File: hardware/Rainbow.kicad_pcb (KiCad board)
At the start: 2 copper layers, 63.3 x 47.9 mm, 22 parts, among them J1 PICKit3, J2 UART, J3 BARREL_JACK, J4 HC-05, J5 RGB, Q1 Q_NMOS_GDS, Q2 Q_NMOS_GDS, Q3 Q_NMOS_GDS, SW1 SWITCH, U1 PIC16F15325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

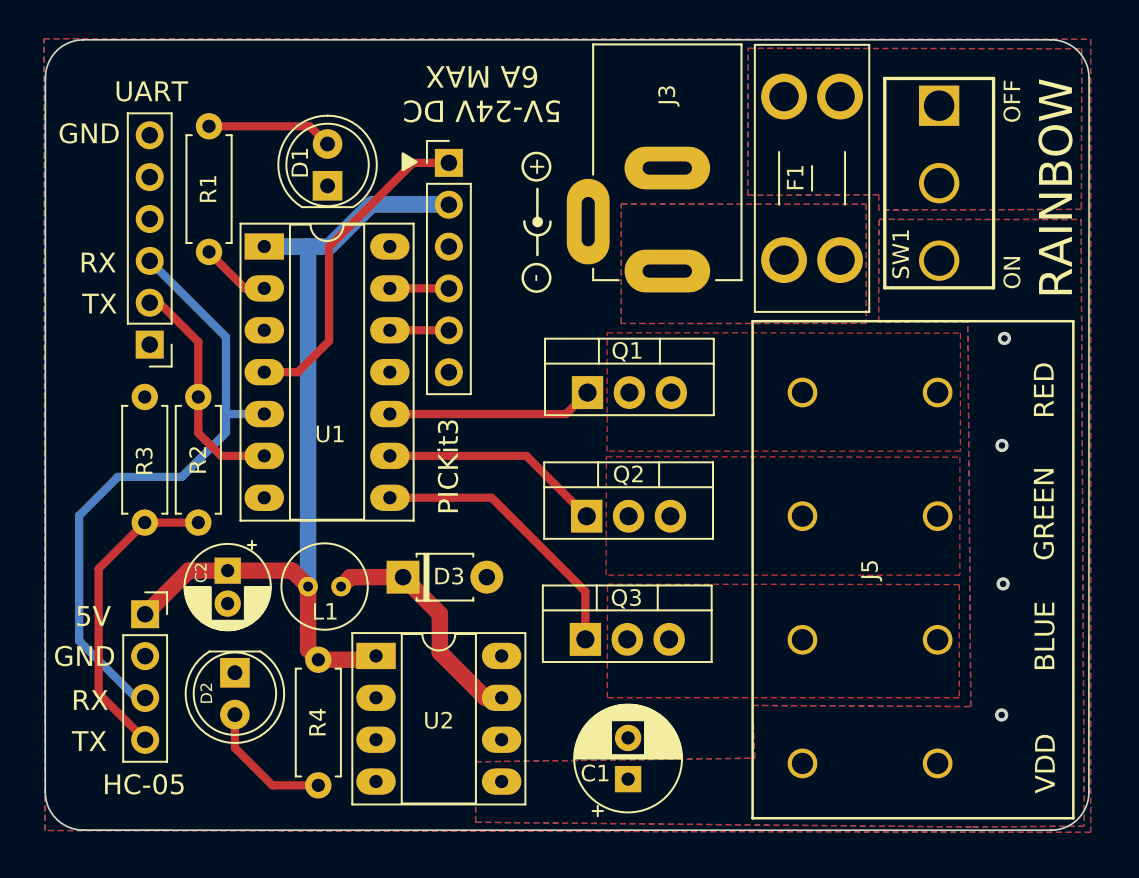
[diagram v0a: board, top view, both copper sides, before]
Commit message: 0.1 uF bypass capacitor
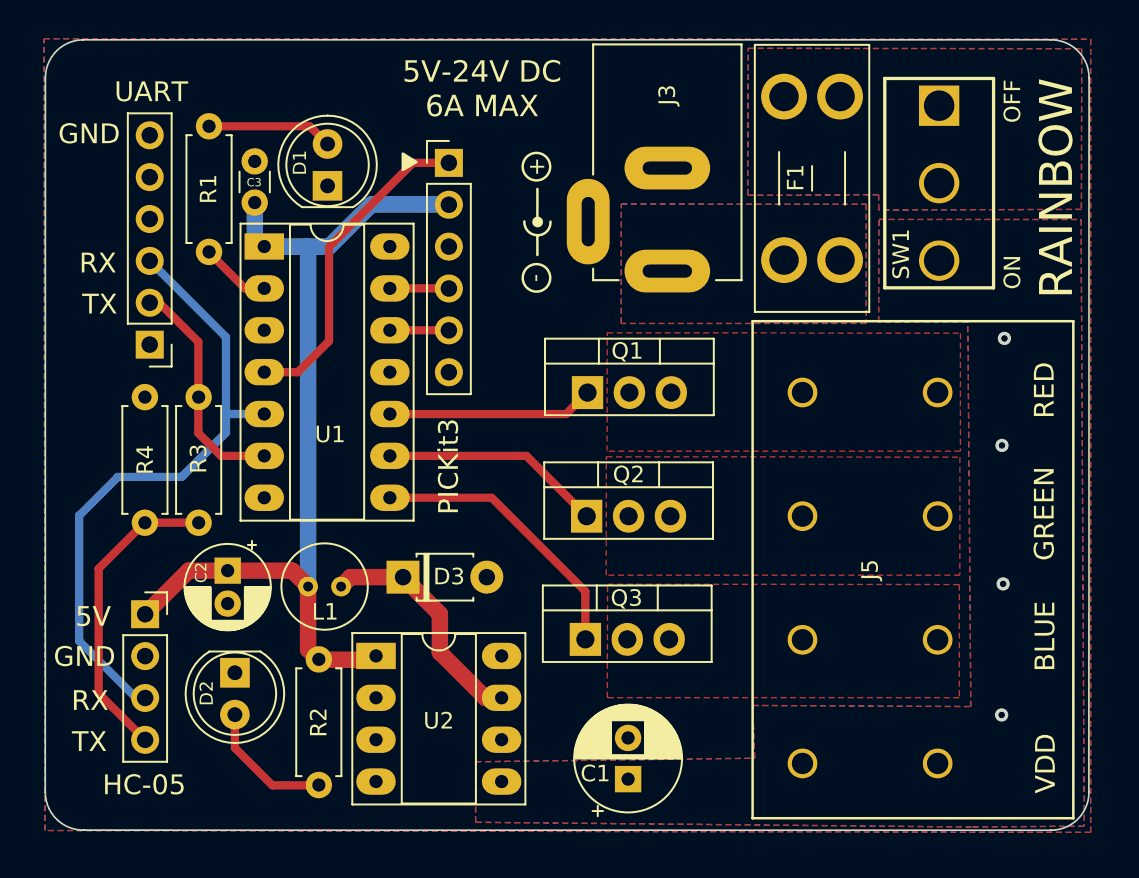
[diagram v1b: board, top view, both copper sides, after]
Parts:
- added C3: 0.1uF, Capacitor_THT:C_Disc_D3.0mm_W1.6mm_P2.50mm, F.Cu at (124.6, 73.2)
- R2: value 1K -> 270R
- R3: value 2K -> 1K
- R4: value 270R -> 2K
- moved R2 17.5 mm to (128.5, 100.9)
- moved R4 13.4 mm to (118.0, 92.7), turned to 90 degrees
- moved R3 8.28 mm to (121.2, 85.0), turned to -90 degrees
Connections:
- R2 pad 1: TX -> +5V
- R2 pad 2: Net-(J4-Pad4) -> Net-(D2-Pad2)
- R3 pad 1: Net-(J4-Pad4) -> TX
- R3 pad 2: GNDREF -> Net-(J4-Pad4)
- R4 pad 1: +5V -> Net-(J4-Pad4)
- R4 pad 2: Net-(D2-Pad2) -> GNDREF
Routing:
- net +5V: track 52.2 -> 55.1 mm
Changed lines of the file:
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@@
+    )
+  )
+  (footprint "Capacitor_THT:C_Disc_D3.0mm_W1.6mm_P2.50mm" (layer "F.Cu")
+    (at 124.63 73.23 90)
+    (descr "C, Disc series, Radial, pin pitch=2.50mm, , diameter*width=3.0*1.6mm^2, Capacitor, http://www.vishay.com/docs/45233/krseries.pdf")
+    (tags "C Disc series Radial pin pitch 2.50mm  diameter 3.0mm width 1.6mm Capacitor")
+    (property "Sheetfile" "Rainbow.kicad_sch")
+    (property "Sheetname" "")
+    (attr through_hole)
+    (fp_text reference "C3" (at 1.22 -0.03 180) (layer "F.SilkS")
+      (effects (font (size 0.5 0.5) (thickness 0.1)))
+    )
+    (fp_text value "0.1uF" (at 1.25 2.05 90) (layer "F.Fab")
+      (effects (font (size 1 1) (thickness 0.15)))
+    )
+    (fp_text user "${REFERENCE}" (at 1.25 0 90) (layer "F.Fab")
+      (effects (font (size 0.6 0.6) (thickness 0.09)))
+    )
+    (fp_line (start 0.621 -0.92) (end 1.879 -0.92) (layer "F.SilkS") (width 0.12))
+    (fp_line (start 0.621 0.92) (end 1.879 0.92) (layer "F.SilkS") (width 0.12))
+    (fp_line (start 3.55 -1.05) (end -1.05 -1.05) (layer "F.CrtYd") (width 0.05))
+    (fp_line (start 3.55 1.05) (end 3.55 -1.05) (layer "F.CrtYd") (width 0.05))
+    (fp_line (start -1.05 1.05) (end 3.55 1.05) (layer "F.CrtYd") (width 0.05))
+    (fp_line (start -1.05 -1.05) (end -1.05 1.05) (layer "F.CrtYd") (width 0.05))
+    (fp_line (start -0.25 -0.8) (end -0.25 0.8) (layer "F.Fab") (width 0.1))
+    (fp_line (start 2.75 0.8) (end 2.75 -0.8) (layer "F.Fab") (width 0.1))
+    (fp_line (start -0.25 0.8) (end 2.75 0.8) (layer "F.Fab") (width 0.1))
+    (fp_line (start 2.75 -0.8) (end -0.25 -0.8) (layer "F.Fab") (width 0.1))
+    (pad "1" thru_hole circle (at 0 0 90) (size 1.6 1.6) (drill 0.8) (layers *.Cu *.Mask)
+      (net 4 "+5V") (pintype "passive"))
+    (pad "2" thru_hole circle (at 2.5 0 90) (size 1.6 1.6) (drill 0.8) (layers *.Cu *.Mask)
+      (net 1 "GNDREF") (pintype "passive"))
+    (model "${KICAD6_3DMODEL_DIR}/Capacitor_THT.3dshapes/C_Disc_D3.0mm_W1.6mm_P2.50mm.wrl"
+      (offset (xyz 0 0 0))
+      (scale (xyz 1 1 1))
+      (rotate (xyz 0 0 0))
     )
   )
   (footprint "Resistor_THT:R_Axial_DIN0207_L6.3mm_D2.5mm_P7.62mm_Horizontal" (layer "F.Cu")
-    (at 128.49 100.96 -90)
+    (at 117.97 92.65 90)
     (descr "Resistor, Axial_DIN0207 series, Axial, Horizontal, pin pitch=7.62mm, 0.25W = 1/4W, length*diameter=6.3*2.5mm^2, http://cdn-reichelt.de/documents/datenblatt/B400/1_4W%23YAG.pdf")
     (tags "Resistor Axial_DIN0207 series Axial Horizontal pin pitch 7.62mm 0.25W = 1/4W length 6.3mm diameter 2.5mm")
@@
       (effects (font (size 1 1) (thickness 0.15)))
     )
-    (fp_text value "270R" (at 3.81 2.37 90) (layer "F.Fab")
+    (fp_text value "2K" (at 3.81 2.37 90) (layer "F.Fab")
       (effects (font (size 1 1) (thickness 0.15)))
     )
@@
     (fp_line (start 0.66 -1.25) (end 0.66 1.25) (layer "F.Fab") (width 0.1))
     (fp_line (start 0.66 1.25) (end 6.96 1.25) (layer "F.Fab") (width 0.1))
-    (pad "1" thru_hole circle (at 0 0 270) (size 1.6 1.6) (drill 0.8) (layers *.Cu *.Mask)
-      (net 4 "+5V") (pintype "passive"))
-    (pad "2" thru_hole oval (at 7.62 0 270) (size 1.6 1.6) (drill 0.8) (layers *.Cu *.Mask)
-      (net 21 "Net-(D2-Pad2)") (pintype "passive"))
+    (pad "1" thru_hole circle (at 0 0 90) (size 1.6 1.6) (drill 0.8) (layers *.Cu *.Mask)
+      (net 24 "Net-(J4-Pad4)") (pintype "passive"))
+    (pad "2" thru_hole oval (at 7.62 0 90) (size 1.6 1.6) (drill 0.8) (layers *.Cu *.Mask)
+      (net 1 "GNDREF") (pintype "passive"))
     (model "${KICAD6_3DMODEL_DIR}/Resistor_THT.3dshapes/R_Axial_DIN0207_L6.3mm_D2.5mm_P7.62mm_Horizontal.wrl"
       (offset (xyz 0 0 0))
@@
     (attr through_hole)
     (fp_text reference "D2" (at 1.245 1.71 90) (layer "F.SilkS")
-      (effects (font (size 0.7 0.7) (thickness 0.15)))
+      (effects (font (size 0.8 0.8) (thickness 0.125)))
     )
     (fp_text value "LED" (at 1.27 3.96 90) (layer "F.Fab")
@@
     (property "Sheetname" "")
     (attr through_hole)
-    (fp_text reference "D1" (at 1.4 -1.65 90) (layer "F.SilkS")
-      (effects (font (size 1 1) (thickness 0.15)))
+    (fp_text reference "D1" (at 1.405 -1.68 90) (layer "F.SilkS")
+      (effects (font (size 0.8 0.8) (thickness 0.125)))
     )
     (fp_text value "LED" (at 1.27 3.96 90) (layer "F.Fab")
@@
   )
   (footprint "Resistor_THT:R_Axial_DIN0207_L6.3mm_D2.5mm_P7.62mm_Horizontal" (layer "F.Cu")
-    (at 121.21 85.02 -90)
+    (at 128.52 100.94 -90)
     (descr "Resistor, Axial_DIN0207 series, Axial, Horizontal, pin pitch=7.62mm, 0.25W = 1/4W, length*diameter=6.3*2.5mm^2, http://cdn-reichelt.de/documents/datenblatt/B400/1_4W%23YAG.pdf")
     (tags "Resistor Axial_DIN0207 series Axial Horizontal pin pitch 7.62mm 0.25W = 1/4W length 6.3mm diameter 2.5mm")
@@
       (effects (font (size 1 1) (thickness 0.15)))
     )
-    (fp_text value "1K" (at 3.81 2.37 90) (layer "F.Fab")
+    (fp_text value "270R" (at 3.81 2.37 90) (layer "F.Fab")
       (effects (font (size 1 1) (thickness 0.15)))
     )
@@
     (fp_line (start 6.96 1.25) (end 6.96 -1.25) (layer "F.Fab") (width 0.1))
     (pad "1" thru_hole circle (at 0 0 270) (size 1.6 1.6) (drill 0.8) (layers *.Cu *.Mask)
-      (net 9 "TX") (pintype "passive"))
+      (net 4 "+5V") (pintype "passive"))
     (pad "2" thru_hole oval (at 7.62 0 270) (size 1.6 1.6) (drill 0.8) (layers *.Cu *.Mask)
-      (net 24 "Net-(J4-Pad4)") (pintype "passive"))
+      (net 21 "Net-(D2-Pad2)") (pintype "passive"))
     (model "${KICAD6_3DMODEL_DIR}/Resistor_THT.3dshapes/R_Axial_DIN0207_L6.3mm_D2.5mm_P7.62mm_Horizontal.wrl"
       (offset (xyz 0 0 0))
@@
   )
   (footprint "Resistor_THT:R_Axial_DIN0207_L6.3mm_D2.5mm_P7.62mm_Horizontal" (layer "F.Cu")
-    (at 117.96 92.64 90)
+    (at 121.23 85.03 -90)
     (descr "Resistor, Axial_DIN0207 series, Axial, Horizontal, pin pitch=7.62mm, 0.25W = 1/4W, length*diameter=6.3*2.5mm^2, http://cdn-reichelt.de/documents/datenblatt/B400/1_4W%23YAG.pdf")
     (tags "Resistor Axial_DIN0207 series Axial Horizontal pin pitch 7.62mm 0.25W = 1/4W length 6.3mm diameter 2.5mm")
@@
       (effects (font (size 1 1) (thickness 0.15)))
     )
-    (fp_text value "2K" (at 3.81 2.37 90) (layer "F.Fab")
+    (fp_text value "1K" (at 3.81 2.37 90) (layer "F.Fab")
       (effects (font (size 1 1) (thickness 0.15)))
     )
@@
     (fp_line (start 0.66 1.25) (end 6.96 1.25) (layer "F.Fab") (width 0.1))
     (fp_line (start 0 0) (end 0.66 0) (layer "F.Fab") (width 0.1))
-    (pad "1" thru_hole circle (at 0 0 90) (size 1.6 1.6) (drill 0.8) (layers *.Cu *.Mask)
+    (pad "1" thru_hole circle (at 0 0 270) (size 1.6 1.6) (drill 0.8) (layers *.Cu *.Mask)
+      (net 9 "TX") (pintype "passive"))
+    (pad "2" thru_hole oval (at 7.62 0 270) (size 1.6 1.6) (drill 0.8) (layers *.Cu *.Mask)
       (net 24 "Net-(J4-Pad4)") (pintype "passive"))
-    (pad "2" thru_hole oval (at 7.62 0 90) (size 1.6 1.6) (drill 0.8) (layers *.Cu *.Mask)
-      (net 1 "GNDREF") (pintype "passive"))
     (model "${KICAD6_3DMODEL_DIR}/Resistor_THT.3dshapes/R_Axial_DIN0207_L6.3mm_D2.5mm_P7.62mm_Horizontal.wrl"
       (offset (xyz 0 0 0))
@@
     (effects (font (size 1.2 1.2) (thickness 0.2)))
   )
-  (gr_text "5V-24V DC\n6A MAX" (at 138.44 66.6 180) (layer "F.SilkS")
+  (gr_text "5V-24V DC\n6A MAX" (at 138.42 66.34) (layer "F.SilkS")
     (effects (font (size 1.3 1.3) (thickness 0.2)))
   )
@@
   (segment (start 127.845 75.895) (end 129.155 75.895) (width 1) (layer "B.Cu") (net 4))
   (segment (start 136.39 73.34) (end 131.71 73.34) (width 1) (layer "B.Cu") (net 4))
+  (segment (start 124.63 75.315) (end 124.63 73.23) (width 1) (layer "B.Cu") (net 4))
+  (segment (start 125.21 75.895) (end 124.63 75.315) (width 1) (layer "B.Cu") (net 4))
   (segment (start 129.155 75.895) (end 131.71 73.34) (width 1) (layer "B.Cu") (net 4))
   (segment (start 132.83 78.435) (end 136.405 78.435) (width 0.5) (layer "F.Cu") (net 5))

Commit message: Change diode footprint
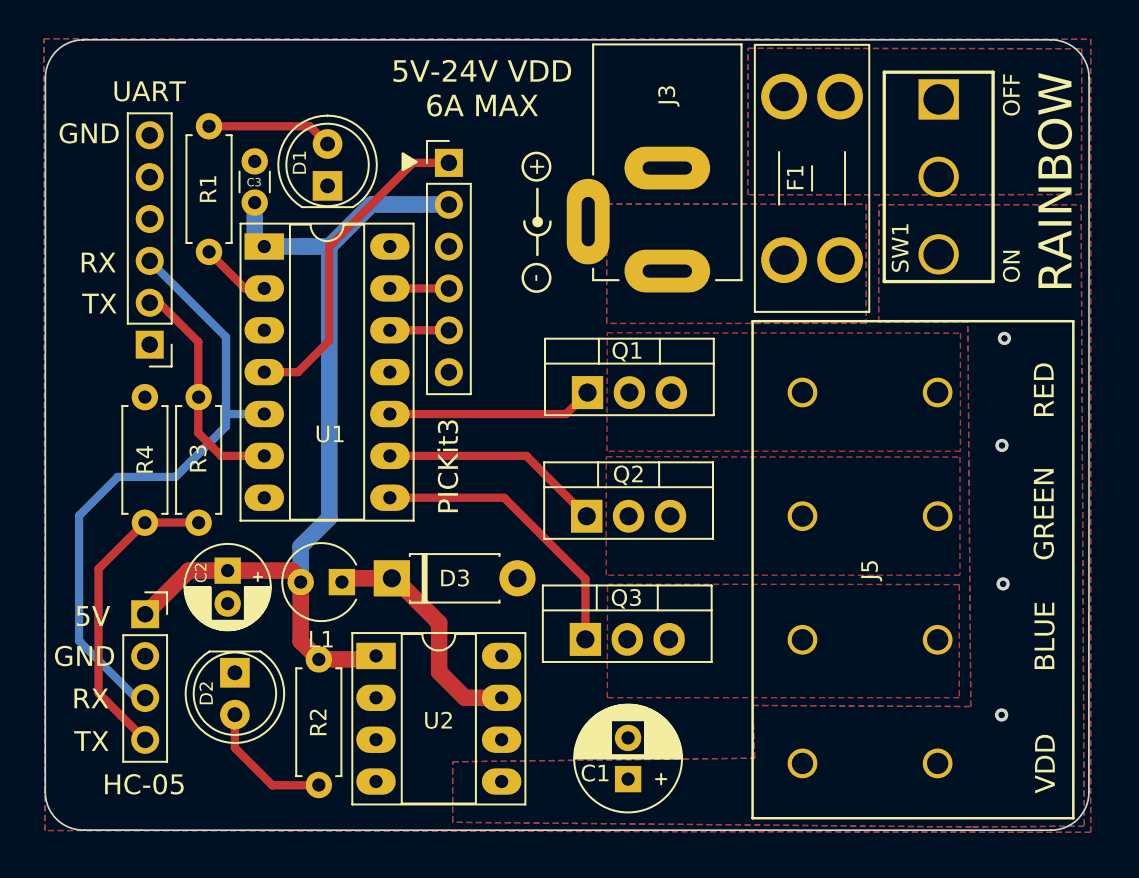
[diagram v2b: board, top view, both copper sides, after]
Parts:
- D3: footprint Diode_THT:D_T-1_P5.08mm_Horizontal -> Diode_THT:D_DO-41_SOD81_P7.62mm_Horizontal
- L1: footprint Capacitor_THT:C_Radial_D5.0mm_H7.0mm_P2.00mm -> Capacitor_THT:CP_Radial_Tantal_D4.5mm_P2.50mm
- moved D3 0.68 mm to (132.9, 96.0)
- moved SW1 0.38 mm to (166.1, 71.7)
- moved L1 0.27 mm to (129.9, 96.2)
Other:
- board text added: "5V-24V VDD 6A MAX"
- board text removed: "5V-24V DC 6A MAX"

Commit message: Diodes for reverse polarity protection
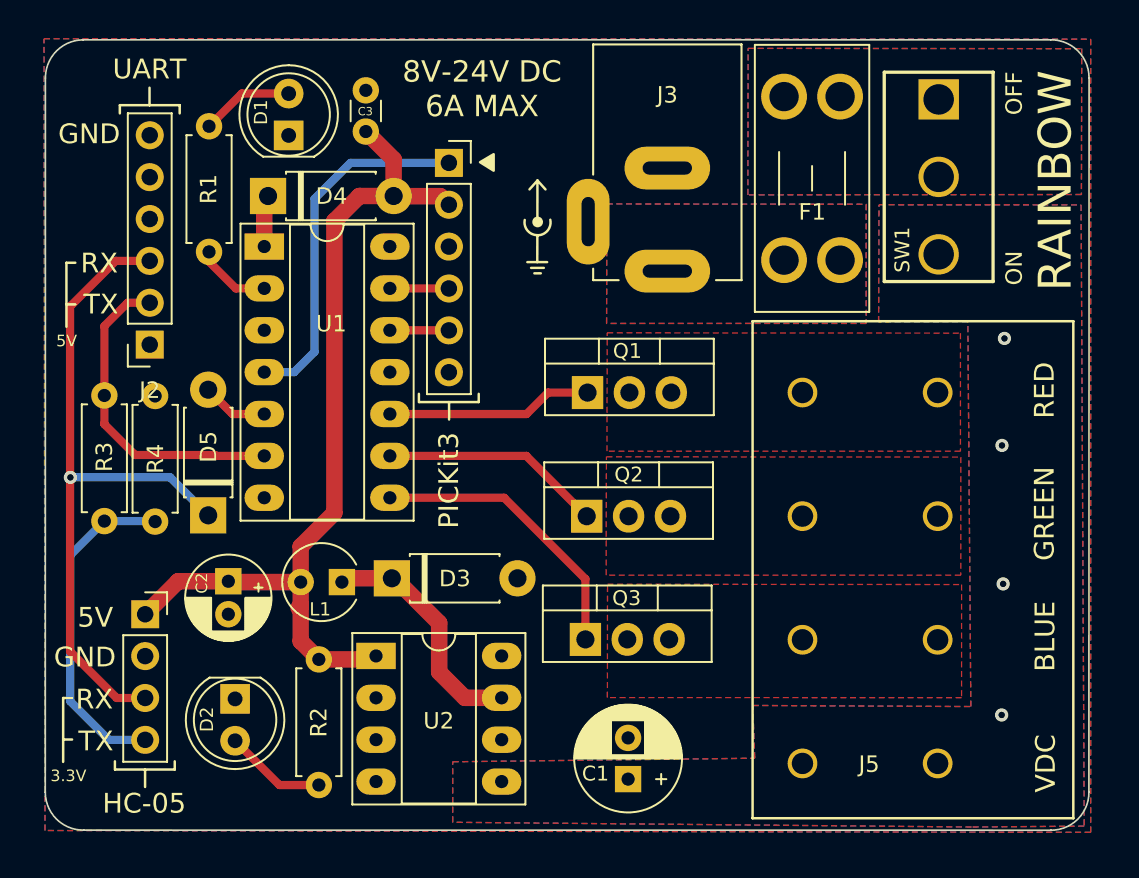
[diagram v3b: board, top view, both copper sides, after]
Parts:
- added D4: 1N5819, Diode_THT:D_DO-41_SOD81_P7.62mm_Horizontal, F.Cu at (125.4, 72.8)
- added D5: 1N5819, Diode_THT:D_DO-41_SOD81_P7.62mm_Horizontal, F.Cu at (121.8, 92.2)
- D3: value D_Schottky -> 1N5819
- J1, J2: footprint Connector_PinHeader_2.54mm:PinHeader_1x06_P2.54mm_Vertical -> Connector_PinSocket_2.54mm:PinSocket_1x06_P2.54mm_Vertical
- moved C3 8.00 mm to (131.4, 68.9)
- moved R3 5.72 mm to (115.5, 84.9)
- moved D1 3.86 mm to (126.7, 69.2)
- moved D2 1.59 mm to (123.4, 103.3)
- moved C2 0.65 mm to (123.0, 96.2)
- moved R4 0.62 mm to (118.6, 92.6)
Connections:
- U1 pad 1: +5V -> Net-(U1-Pad1)
- U1 pad 5: RX -> Net-(U1-Pad5)
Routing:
- net TX: track 13.5 -> 19.8 mm
- net RX: track 37.9 -> 42.1 mm, vias 0 -> 1
- net Net-(U1-Pad5): track 0.00 -> 4.01 mm
- net Net-(U1-Pad1): track 0.00 -> 3.16 mm
- net MCLR: track 19.8 -> 21.9 mm
- net Net-(D1-Pad2): track 7.64 -> 5.65 mm
- net Net-(D2-Pad2): track 8.02 -> 6.19 mm
- net Net-(J4-Pad4): track 18.8 -> 20.4 mm
- net +5V: track 55.5 -> 54.0 mm
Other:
- board text added: "3.3V"
- board text added: "8V-24V DC 6A MAX"
- board text added: "VDC"
- board text removed: "+"
- board text removed: "-"
- board text removed: "5V-24V VDD 6A MAX"
- board text removed: "VDD"

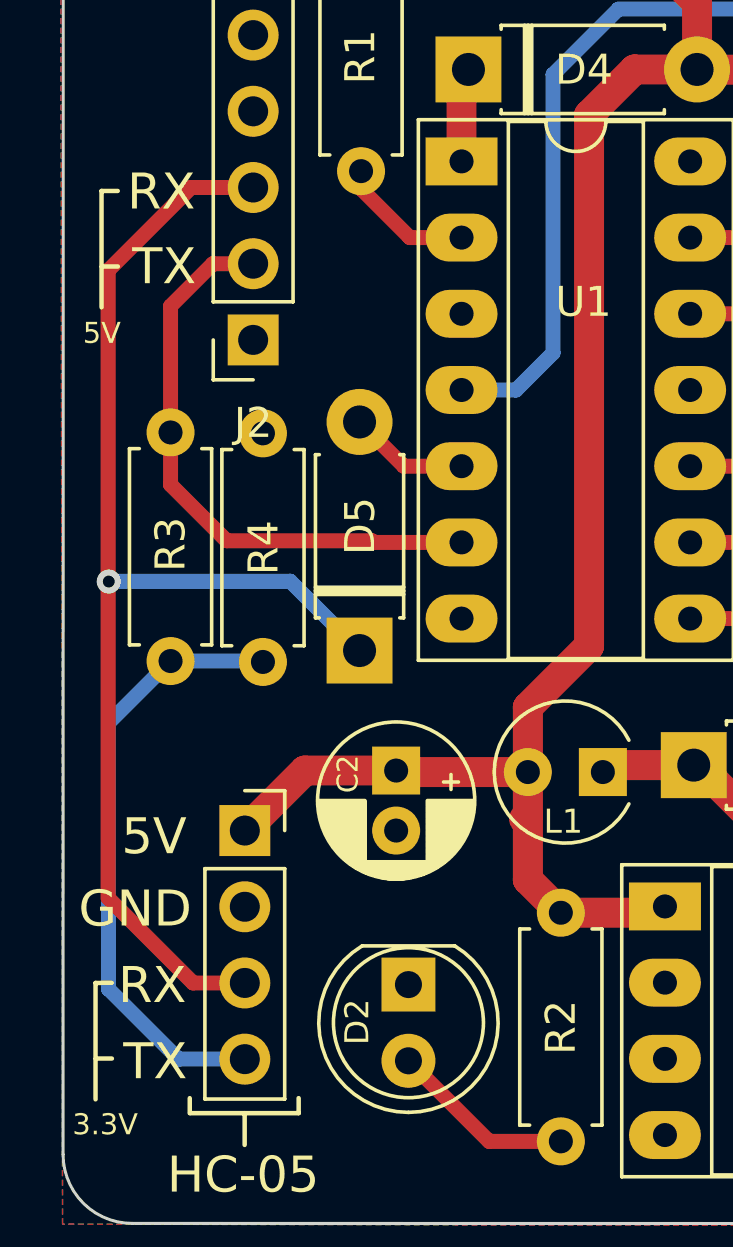
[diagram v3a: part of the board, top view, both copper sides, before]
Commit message: Remove extra diode on RX line
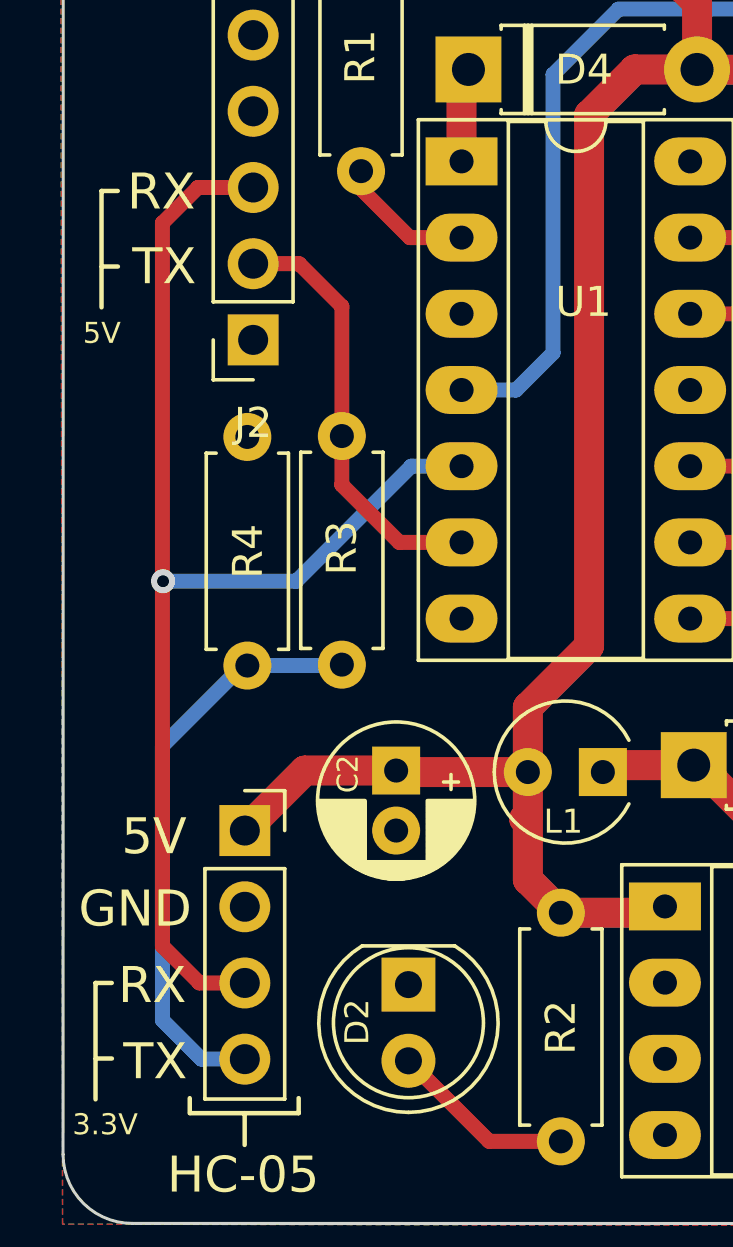
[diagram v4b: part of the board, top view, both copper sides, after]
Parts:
- removed D5: 1N5819, Diode_THT:D_DO-41_SOD81_P7.62mm_Horizontal
- moved R3 5.71 mm to (121.2, 85.0)
- moved R4 0.53 mm to (118.1, 92.7)
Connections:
- U1 pad 5: Net-(U1-Pad5) -> RX
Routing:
- net TX: track 19.8 -> 14.3 mm
- net Net-(U1-Pad5): track 4.01 -> 0.00 mm
- net Net-(J4-Pad4): track 20.4 -> 19.6 mm
